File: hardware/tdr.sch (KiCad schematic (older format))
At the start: 0 parts

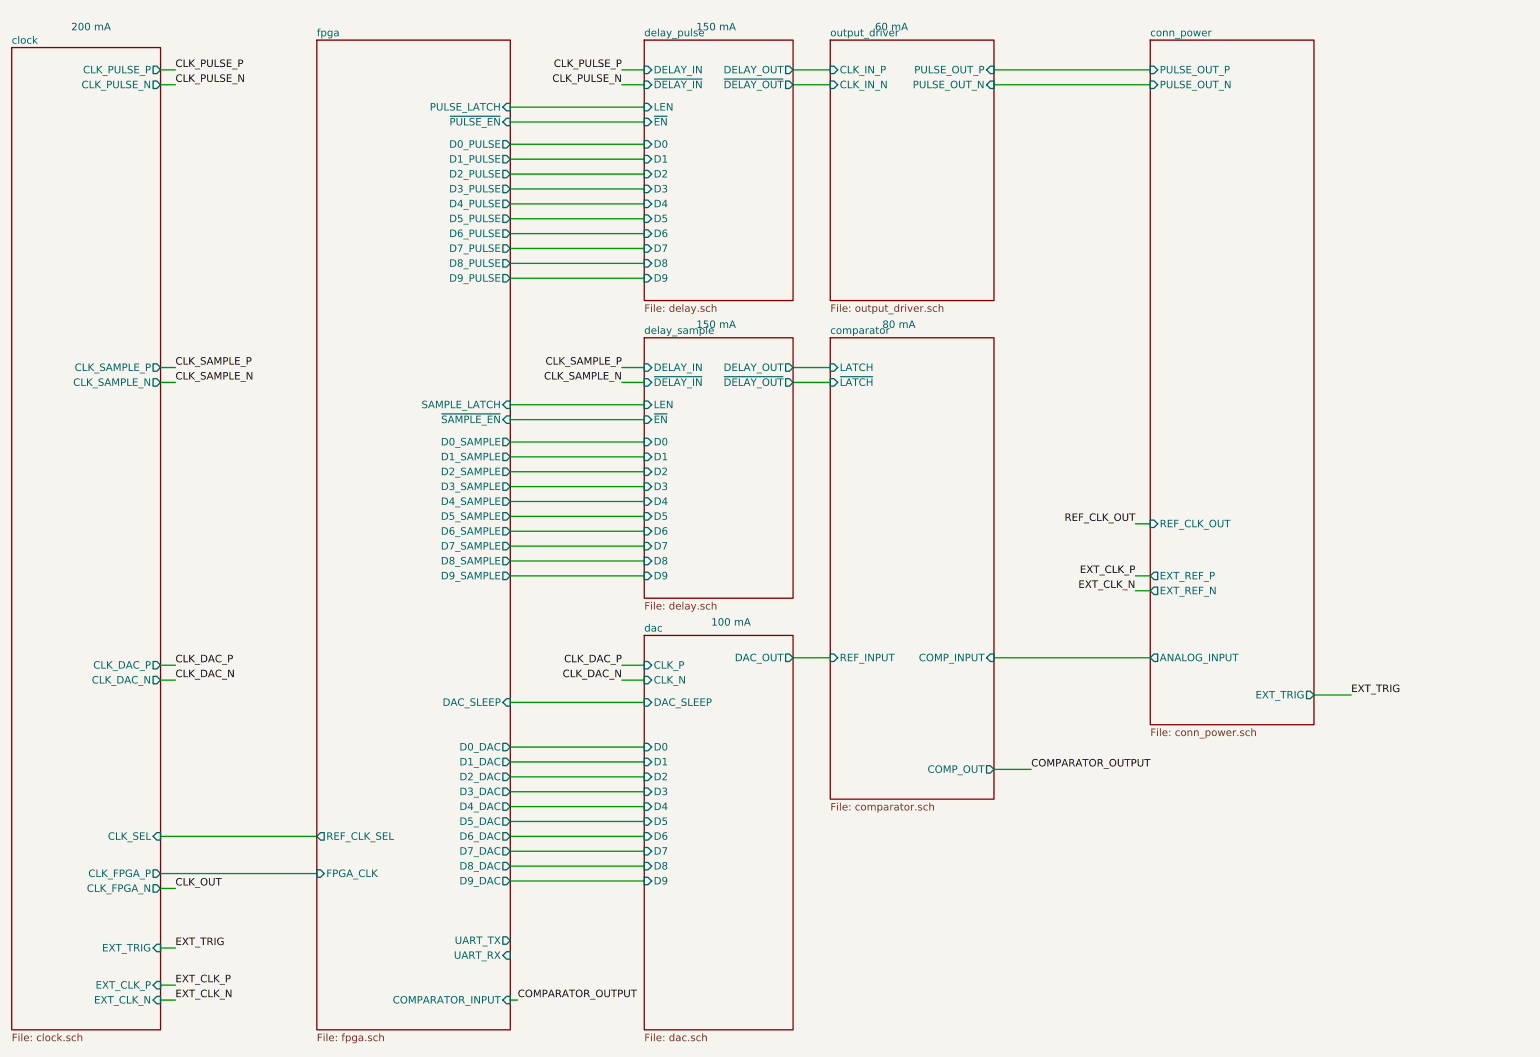
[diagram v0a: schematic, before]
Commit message: more work on tdr schematic
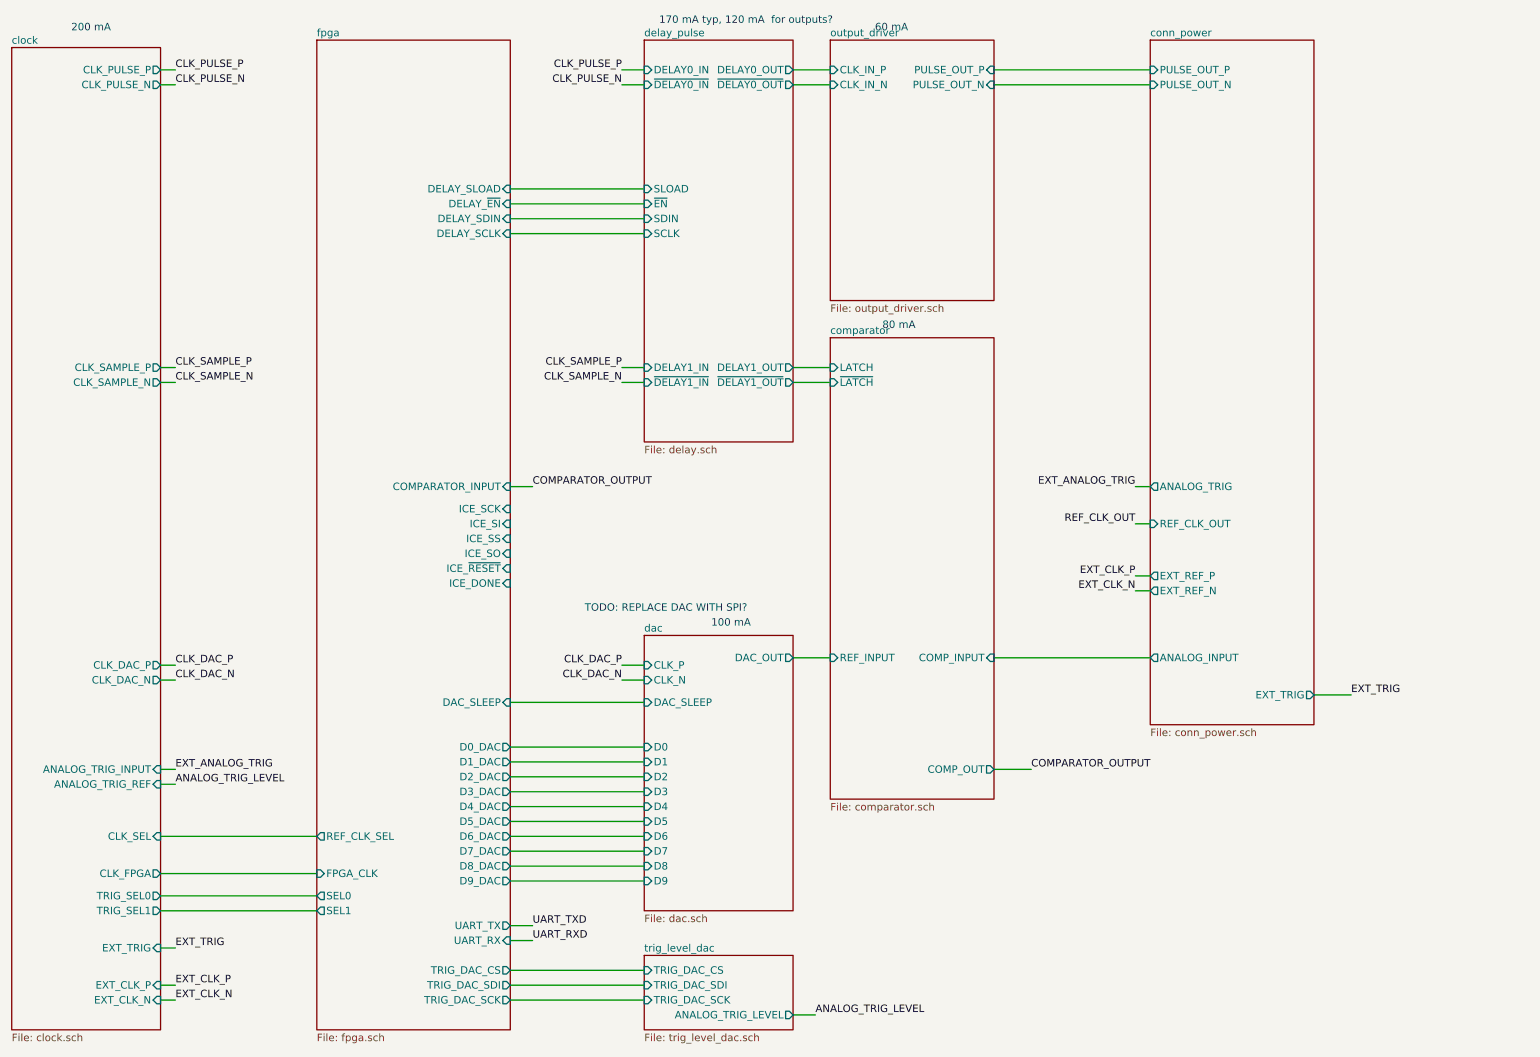
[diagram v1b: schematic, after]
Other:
- note added: "170 mA typ, 120 mA for outputs?"
- note added: "TODO: REPLACE DAC WITH SPI?"
- note removed: "150 mA"

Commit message: work on tdr schematic..
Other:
- note removed: "100 mA"
- note removed: "TODO: REPLACE DAC WITH SPI?"
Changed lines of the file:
@@
 $Descr A4 11693 8268
 encoding utf-8
-Sheet 1 9
+Sheet 1 8
 Title ""
 Date ""
@@
 Text Label 4850 3050 2    50   ~ 0
 CLK_SAMPLE_N
-Text Label 4850 4950 2    50   ~ 0
-CLK_DAC_P
-Text Label 4850 5050 2    50   ~ 0
-CLK_DAC_N
 Wire Wire Line
 	4850 950  5000 950
@@
 	4850 3050 5000 3050
 Wire Wire Line
-	4850 4950 5000 4950
-Wire Wire Line
-	4850 5050 5000 5050
-Wire Wire Line
 	8300 4350 8400 4350
 Wire Wire Line
 	8300 4450 8400 4450
-$Sheet
-S 2800 750  1300 6650
-U 5BC3F67C
-F0 "fpga" 50
-F1 "fpga.sch" 50
-F2 "D0_DAC" O R 4100 5500 50
-F3 "D1_DAC" O R 4100 5600 50
-F4 "D2_DAC" O R 4100 5700 50
-F5 "D3_DAC" O R 4100 5800 50
-F6 "D4_DAC" O R 4100 5900 50
-F7 "D5_DAC" O R 4100 6000 50
-F8 "D6_DAC" O R 4100 6100 50
-F9 "D7_DAC" O R 4100 6200 50
-F10 "D8_DAC" O R 4100 6300 50
-F11 "D9_DAC" O R 4100 6400 50
-F12 "DAC_SLEEP" I R 4100 5200 50
-F13 "COMPARATOR_INPUT" I R 4100 3750 50
-F14 "REF_CLK_SEL" O L 2800 6100 50
-F15 "UART_TX" O R 4100 6700 50
-F16 "UART_RX" I R 4100 6800 50
-F17 "FPGA_CLK" I L 2800 6350 50
-F18 "ICE_SCK" I R 4100 3900 50
-F19 "ICE_SI" I R 4100 4000 50
-F20 "ICE_SS" I R 4100 4100 50
-F21 "ICE_SO" I R 4100 4200 50
-F22 "ICE_~RESET" I R 4100 4300 50
-F23 "ICE_DONE" I R 4100 4400 50
-F24 "DELAY_SLOAD" I R 4100 1750 50
-F25 "DELAY_~EN" I R 4100 1850 50
-F26 "DELAY_SDIN" I R 4100 1950 50
-F27 "DELAY_SCLK" I R 4100 2050 50
-F28 "SEL1" O L 2800 6600 50
-F29 "SEL0" O L 2800 6500 50
-F30 "TRIG_DAC_SCK" O R 4100 7200 50
-F31 "TRIG_DAC_SDI" O R 4100 7100 50
-F32 "TRIG_DAC_CS" O R 4100 7000 50
-$EndSheet
-Wire Wire Line
-	4100 5500 5000 5500
-Wire Wire Line
-	4100 5600 5000 5600
-Wire Wire Line
-	4100 5700 5000 5700
-Wire Wire Line
-	4100 5800 5000 5800
-Wire Wire Line
-	4100 5900 5000 5900
-Wire Wire Line
-	4100 6000 5000 6000
-Wire Wire Line
-	4100 6100 5000 6100
-Wire Wire Line
-	4100 6200 5000 6200
-Wire Wire Line
-	4100 6300 5000 6300
-Wire Wire Line
-	4100 6400 5000 6400
 Text Label 4250 3750 0    50   ~ 0
 COMPARATOR_OUTPUT
-Wire Wire Line
-	4100 5200 5000 5200
 Text Notes 1150 700  0    50   ~ 0
 200 mA
 Text Notes 5100 650  0    50   ~ 0
 170 mA typ, 120 mA  for outputs?
-Text Notes 5450 4700 0    50   ~ 0
-100 mA
 Text Notes 6550 700  0    50   ~ 0
 60 mA
@@
 Wire Wire Line
 	5000 2050 4100 2050
-$Sheet
-S 5000 4750 1000 1850
-U 5BC349EC
-F0 "dac" 50
-F1 "dac.sch" 50
-F2 "CLK_P" I L 5000 4950 50
-F3 "CLK_N" I L 5000 5050 50
-F4 "D0" I L 5000 5500 50
-F5 "D1" I L 5000 5600 50
-F6 "D2" I L 5000 5700 50
-F7 "D3" I L 5000 5800 50
-F8 "D4" I L 5000 5900 50
-F9 "D5" I L 5000 6000 50
-F10 "D6" I L 5000 6100 50
-F11 "D7" I L 5000 6200 50
-F12 "D8" I L 5000 6300 50
-F13 "D9" I L 5000 6400 50
-F14 "DAC_SLEEP" I L 5000 5200 50
-F15 "DAC_OUT" O R 6000 4900 50
-$EndSheet
 $Sheet
 S 5000 750  1000 2700
@@
 F13 "SCLK" I L 5000 2050 50
 $EndSheet
-Text Notes 4600 4600 0    50   ~ 0
-TODO: REPLACE DAC WITH SPI?
 Wire Wire Line
 	1750 6500 2800 6500
@@
 Wire Wire Line
 	1850 5750 1750 5750
-Text Label 6150 7300 0    50   ~ 0
+Text Label 6150 6300 0    50   ~ 0
 ANALOG_TRIG_LEVEL
-$Sheet
-S 5000 6900 1000 500
-U 5C1101FF
-F0 "trig_level_dac" 50
+Wire Wire Line
+	4100 3750 4250 3750
+$Sheet
+S 5000 4500 1000 2050
+U 5C262FB6
+F0 "sheet5C262FB0" 50
 F1 "trig_level_dac.sch" 50
-F2 "ANALOG_TRIG_LEVEL" O R 6000 7300 50
-F3 "TRIG_DAC_SCK" I L 5000 7200 50
-F4 "TRIG_DAC_SDI" I L 5000 7100 50
-F5 "TRIG_DAC_CS" I L 5000 7000 50
-$EndSheet
-Wire Wire Line
-	4100 3750 4250 3750
-Wire Wire Line
-	6150 7300 6000 7300
-Wire Wire Line
-	4100 6700 4250 6700
-Text Label 4250 6700 0    50   ~ 0
-UART_TXD
-Text Label 4250 6800 0    50   ~ 0
-UART_RXD
-Wire Wire Line
-	4250 6800 4100 6800
-Wire Wire Line
-	4100 7000 5000 7000
-Wire Wire Line
-	5000 7100 4100 7100
-Wire Wire Line
-	4100 7200 5000 7200
+F2 "DAC_CS" I L 5000 4600 50
+F3 "DAC_SCK" I L 5000 4800 50
+F4 "DAC_SDI" I L 5000 4700 50
+F5 "DAC_VOUT" I R 6000 4900 50
+F6 "TRIG_VOUT" O R 6000 6300 50
+$EndSheet
+Wire Wire Line
+	5000 4600 4100 4600
+$Sheet
+S 2800 750  1300 6650
+U 5BC3F67C
+F0 "fpga_connector" 50
+F1 "fpga.sch" 50
+F2 "COMPARATOR_INPUT" I R 4100 3750 50
+F3 "REF_CLK_SEL" O L 2800 6100 50
+F4 "FPGA_CLK" I L 2800 6350 50
+F5 "DELAY_SLOAD" I R 4100 1750 50
+F6 "DELAY_~EN" I R 4100 1850 50
+F7 "DELAY_SDIN" I R 4100 1950 50
+F8 "DELAY_SCLK" I R 4100 2050 50
+F9 "SEL1" O L 2800 6600 50
+F10 "SEL0" O L 2800 6500 50
+F11 "DAC_SCK" O R 4100 4800 50
+F12 "DAC_SDI" O R 4100 4700 50
+F13 "DAC_CS" O R 4100 4600 50
+$EndSheet
+Wire Wire Line
+	6000 6300 6150 6300
+Wire Wire Line
+	4100 4700 5000 4700
+Wire Wire Line
+	4100 4800 5000 4800
 $EndSCHEMATC

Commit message: work on schematic..
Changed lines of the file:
@@
 F8 "REF_CLK_OUT" I L 8400 4000 50
 F9 "ANALOG_TRIG" O L 8400 3750 50
+F10 "PGOOD_3V3" O L 8400 3400 50
 $EndSheet
 $Sheet
@@
 F5 "DAC_VOUT" I R 6000 4900 50
 F6 "TRIG_VOUT" O R 6000 6300 50
+F7 "DAC_~CLR" I L 5000 4900 50
 $EndSheet
 Wire Wire Line
@@
 F0 "fpga_connector" 50
 F1 "fpga.sch" 50
-F2 "COMPARATOR_INPUT" I R 4100 3750 50
+F2 "COMPARATOR_OUTPUT" I R 4100 3750 50
 F3 "REF_CLK_SEL" O L 2800 6100 50
 F4 "FPGA_CLK" I L 2800 6350 50
@@
 F12 "DAC_SDI" O R 4100 4700 50
 F13 "DAC_CS" O R 4100 4600 50
+F14 "PGOOD_3V3" I R 4100 7150 50
+F15 "DAC_~CLR" O R 4100 4900 50
 $EndSheet
 Wire Wire Line
@@
 Wire Wire Line
 	4100 4800 5000 4800
+Wire Wire Line
+	8400 3400 8300 3400
+Text Label 8300 3400 2    50   ~ 0
+PGOOD_3V3
+Text Label 4350 7150 0    50   ~ 0
+PGOOD_3V3
+Wire Wire Line
+	4350 7150 4100 7150
+Wire Wire Line
+	4100 4900 5000 4900
 $EndSCHEMATC

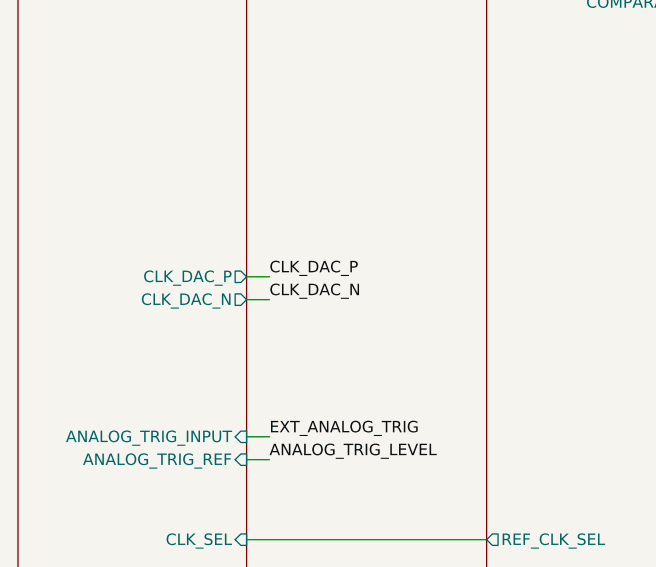
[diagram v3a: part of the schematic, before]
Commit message: work on tdr component placement
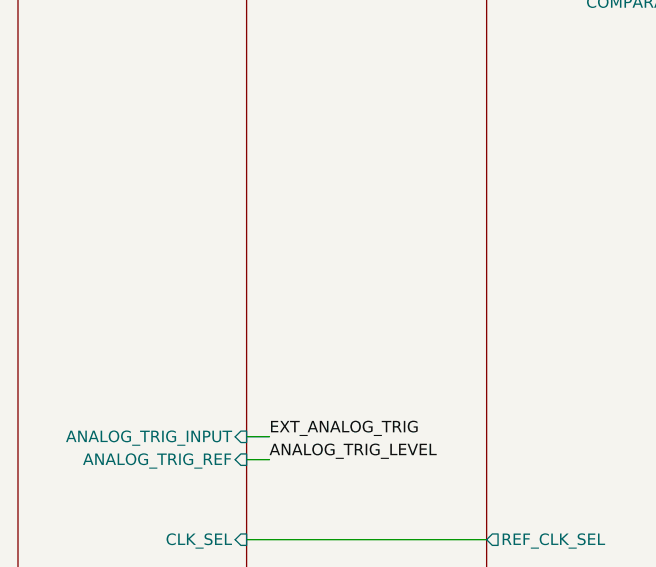
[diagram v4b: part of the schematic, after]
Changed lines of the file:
@@
 F2 "EXT_CLK_P" I R 1750 7100 50
 F3 "EXT_CLK_N" I R 1750 7200 50
-F4 "CLK_DAC_P" O R 1750 4950 50
-F5 "CLK_DAC_N" O R 1750 5050 50
-F6 "CLK_PULSE_P" O R 1750 950 50
-F7 "CLK_PULSE_N" O R 1750 1050 50
-F8 "CLK_SAMPLE_P" O R 1750 2950 50
-F9 "CLK_SEL" I R 1750 6100 50
-F10 "EXT_TRIG" I R 1750 6850 50
-F11 "CLK_SAMPLE_N" O R 1750 3050 50
-F12 "CLK_FPGA" O R 1750 6350 50
-F13 "ANALOG_TRIG_INPUT" I R 1750 5650 50
-F14 "ANALOG_TRIG_REF" I R 1750 5750 50
-F15 "TRIG_SEL1" O R 1750 6600 50
-F16 "TRIG_SEL0" O R 1750 6500 50
+F4 "CLK_PULSE_P" O R 1750 950 50
+F5 "CLK_PULSE_N" O R 1750 1050 50
+F6 "CLK_SAMPLE_P" O R 1750 2950 50
+F7 "CLK_SEL" I R 1750 6100 50
+F8 "EXT_TRIG" I R 1750 6850 50
+F9 "CLK_SAMPLE_N" O R 1750 3050 50
+F10 "CLK_FPGA" O R 1750 6350 50
+F11 "ANALOG_TRIG_INPUT" I R 1750 5650 50
+F12 "ANALOG_TRIG_REF" I R 1750 5750 50
+F13 "TRIG_SEL1" O R 1750 6600 50
+F14 "TRIG_SEL0" O R 1750 6500 50
 $EndSheet
 $Sheet
@@
 	1850 6850 1750 6850
 Wire Wire Line
-	1850 5050 1750 5050
-Text Label 1850 4950 0    50   ~ 0
-CLK_DAC_P
-Wire Wire Line
-	1850 4950 1750 4950
-Text Label 1850 5050 0    50   ~ 0
-CLK_DAC_N
-Wire Wire Line
 	1850 3050 1750 3050

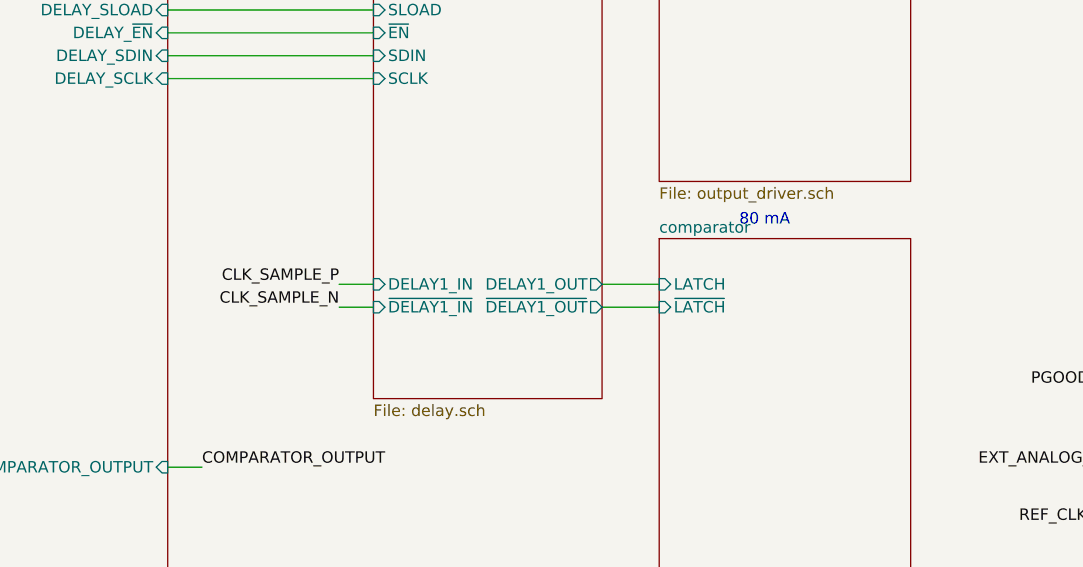
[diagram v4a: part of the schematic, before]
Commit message: added rf crossover for latch trigger line to help with layout
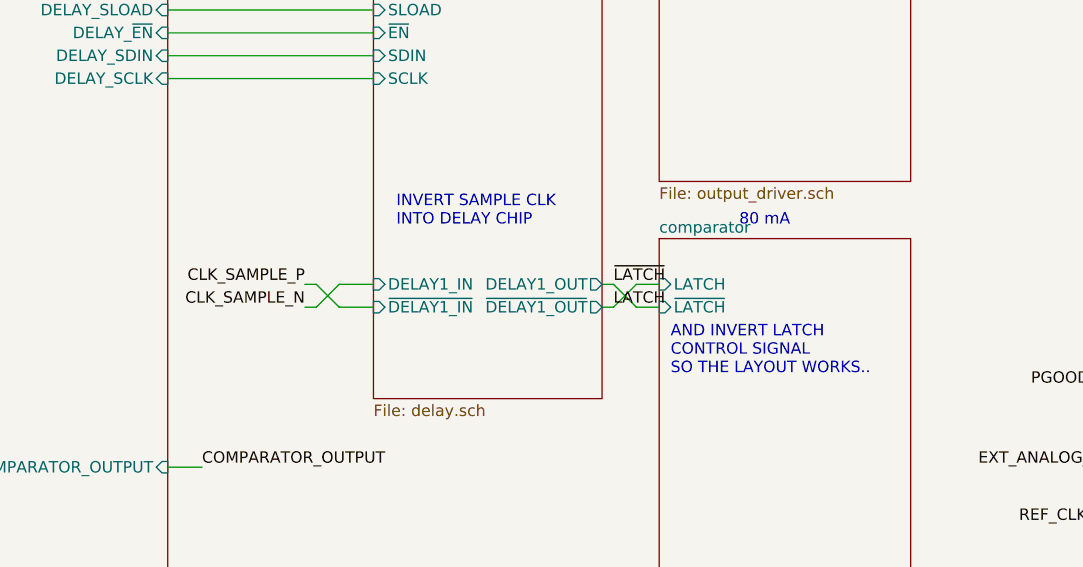
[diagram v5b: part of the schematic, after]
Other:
- note added: "AND INVERT LATCH\nCONTROL SIGNAL\nSO THE LAYOUT WORKS.."
- note added: "INVERT SAMPLE CLK\nINTO DELAY CHIP"
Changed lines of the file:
@@
 	6000 1050 6250 1050
-Wire Wire Line
-	6000 2950 6250 2950
-Wire Wire Line
-	6000 3050 6250 3050
 Wire Wire Line
 	6000 4900 6250 4900
@@
 Text Label 4850 1050 2    50   ~ 0
 CLK_PULSE_N
-Text Label 4850 2950 2    50   ~ 0
+Text Label 4700 2950 2    50   ~ 0
 CLK_SAMPLE_P
-Text Label 4850 3050 2    50   ~ 0
+Text Label 4700 3050 2    50   ~ 0
 CLK_SAMPLE_N
 Wire Wire Line
@@
 Wire Wire Line
 	4100 4900 5000 4900
+Text Notes 5100 2700 0    50   ~ 0
+INVERT SAMPLE CLK\nINTO DELAY CHIP
+Text Notes 6300 3350 0    50   ~ 0
+AND INVERT LATCH\nCONTROL SIGNAL\nSO THE LAYOUT WORKS..
+Wire Wire Line
+	4700 3050 4750 3050
+Wire Wire Line
+	4750 3050 4850 2950
+Wire Wire Line
+	4700 2950 4750 2950
+Wire Wire Line
+	4750 2950 4850 3050
+Wire Wire Line
+	6000 3050 6050 3050
+Wire Wire Line
+	6050 3050 6150 2950
+Wire Wire Line
+	6150 2950 6250 2950
+Wire Wire Line
+	6000 2950 6050 2950
+Wire Wire Line
+	6050 2950 6150 3050
+Wire Wire Line
+	6150 3050 6250 3050
+Text Label 6050 2950 0    50   ~ 0
+~LATCH
+Text Label 6050 3050 0    50   ~ 0
+LATCH
 $EndSCHEMATC

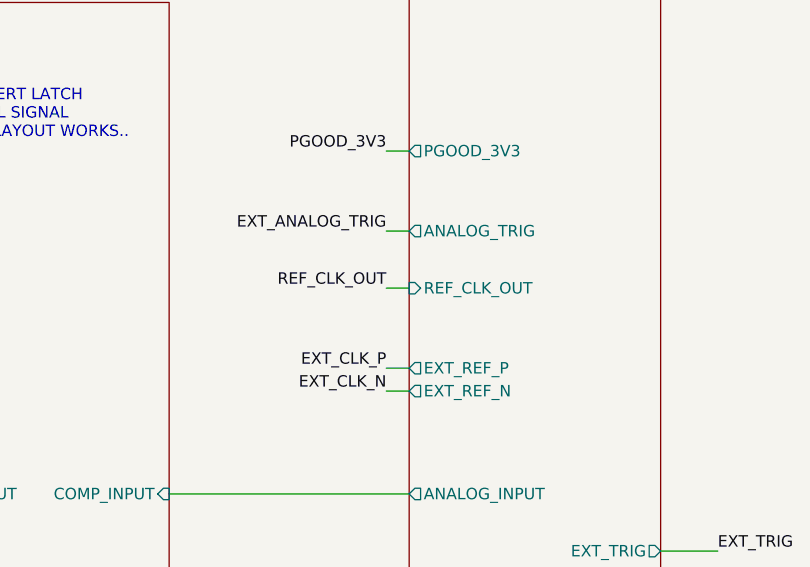
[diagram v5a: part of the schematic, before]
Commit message: finished first pass component placement and drc setup, swapped digital pins for easier routing
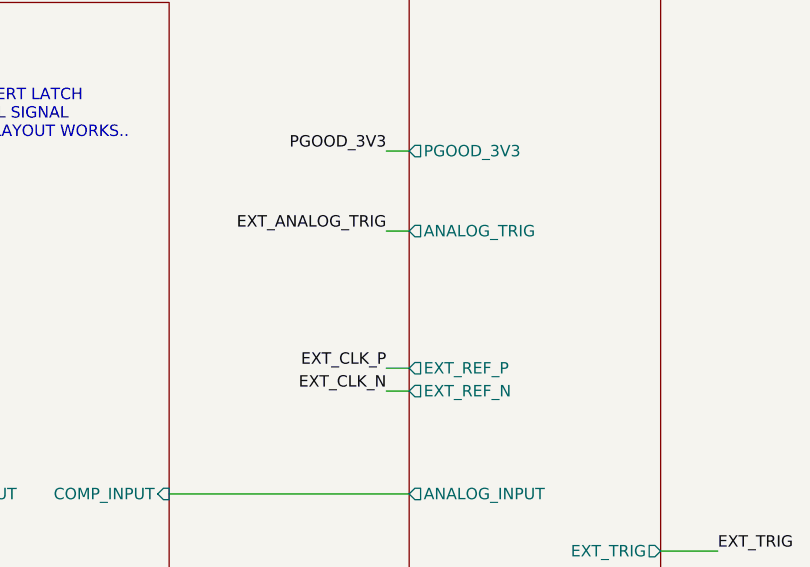
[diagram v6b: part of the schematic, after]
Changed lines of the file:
@@
 F6 "EXT_REF_P" O L 8400 4350 50
 F7 "EXT_REF_N" O L 8400 4450 50
-F8 "REF_CLK_OUT" I L 8400 4000 50
-F9 "ANALOG_TRIG" O L 8400 3750 50
-F10 "PGOOD_3V3" O L 8400 3400 50
+F8 "ANALOG_TRIG" O L 8400 3750 50
+F9 "PGOOD_3V3" O L 8400 3400 50
 $EndSheet
 $Sheet
@@
 Wire Wire Line
 	1750 6350 2800 6350
-Text Label 8300 4000 2    50   ~ 0
-REF_CLK_OUT
-Wire Wire Line
-	8300 4000 8400 4000
 Wire Wire Line
 	4100 1750 5000 1750
